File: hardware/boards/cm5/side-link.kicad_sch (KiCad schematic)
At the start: 2 parts, among them J201 05A20L24P

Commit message: feat(cm5): take the side link on a vertical FH12 at the right edge
J201 becomes a Hirose FH12-24S-0.5SVA(54), contacts toward the right edge with its lands 0.3 mm from it, pin 1 at the front end; main pin n still meets J201 pin 25 - n.
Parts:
- J201: value 05A20L24P -> FH12-24S-0.5SVA(54); footprint Iasis:HanElectricity_05A20L24P -> Iasis:Hirose_FH12-24S-0.5SVA_1x24-1MP_P0.50mm_Vertical; LCSC C5362158 -> C3169218; MPN 05A20L24P -> FH12-24S-0.5SVA(54); Manufacturer HanElectricity -> Hirose
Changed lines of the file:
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@@
 			(effects (font (size 1.27 1.27)) (justify left))
 		)
-		(property "Value" "05A20L24P"
+		(property "Value" "FH12-24S-0.5SVA(54)"
 			(at 99.06 101.6 0)
 			(show_name no)
@@
 			(effects (font (size 1.27 1.27)) (justify left))
 		)
-		(property "Footprint" "Iasis:HanElectricity_05A20L24P"
+		(property "Footprint" "Iasis:Hirose_FH12-24S-0.5SVA_1x24-1MP_P0.50mm_Vertical"
 			(at 101.6 99.06 0)
 			(hide yes)
@@
 			)
 		)
-		(property "LCSC" "C5362158"
+		(property "LCSC" "C3169218"
 			(at 101.6 99.06 0)
 			(hide yes)
@@
 			)
 		)
-		(property "MPN" "05A20L24P"
+		(property "MPN" "FH12-24S-0.5SVA(54)"
 			(at 101.6 99.06 0)
 			(hide yes)
@@
 			)
 		)
-		(property "Manufacturer" "HanElectricity"
+		(property "Manufacturer" "Hirose"
 			(at 101.6 99.06 0)
 			(hide yes)

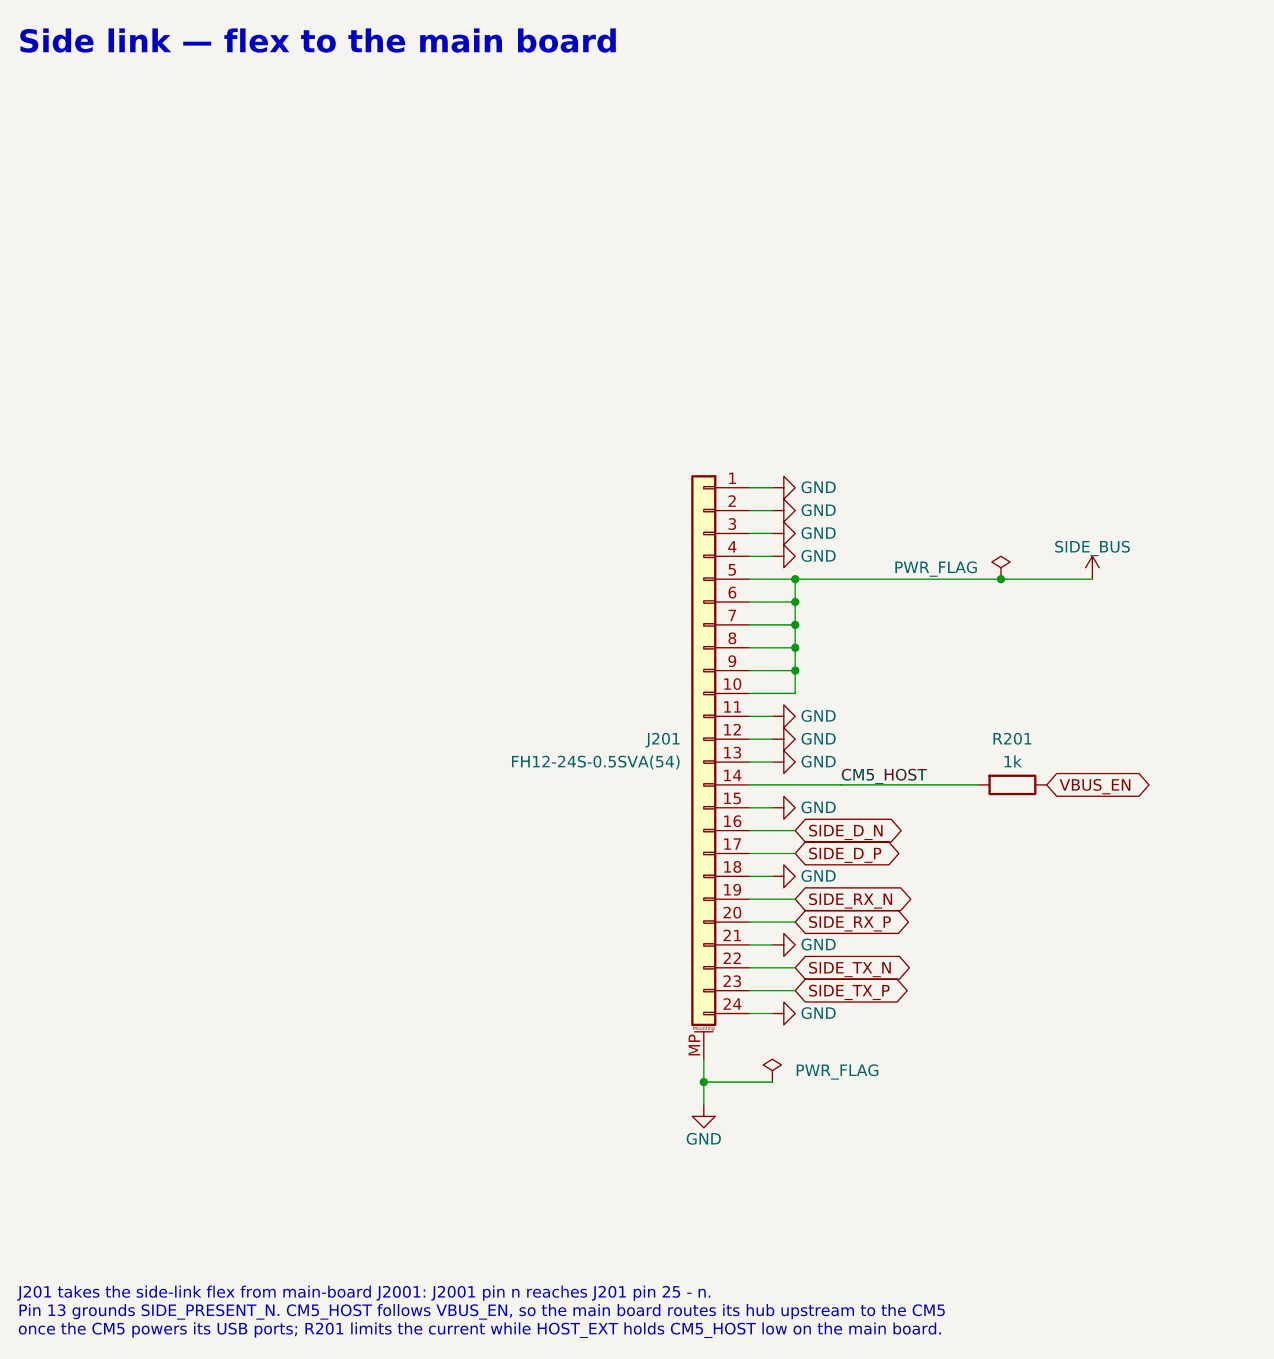
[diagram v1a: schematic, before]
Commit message: feat(hardware): use stocked CM5 headers
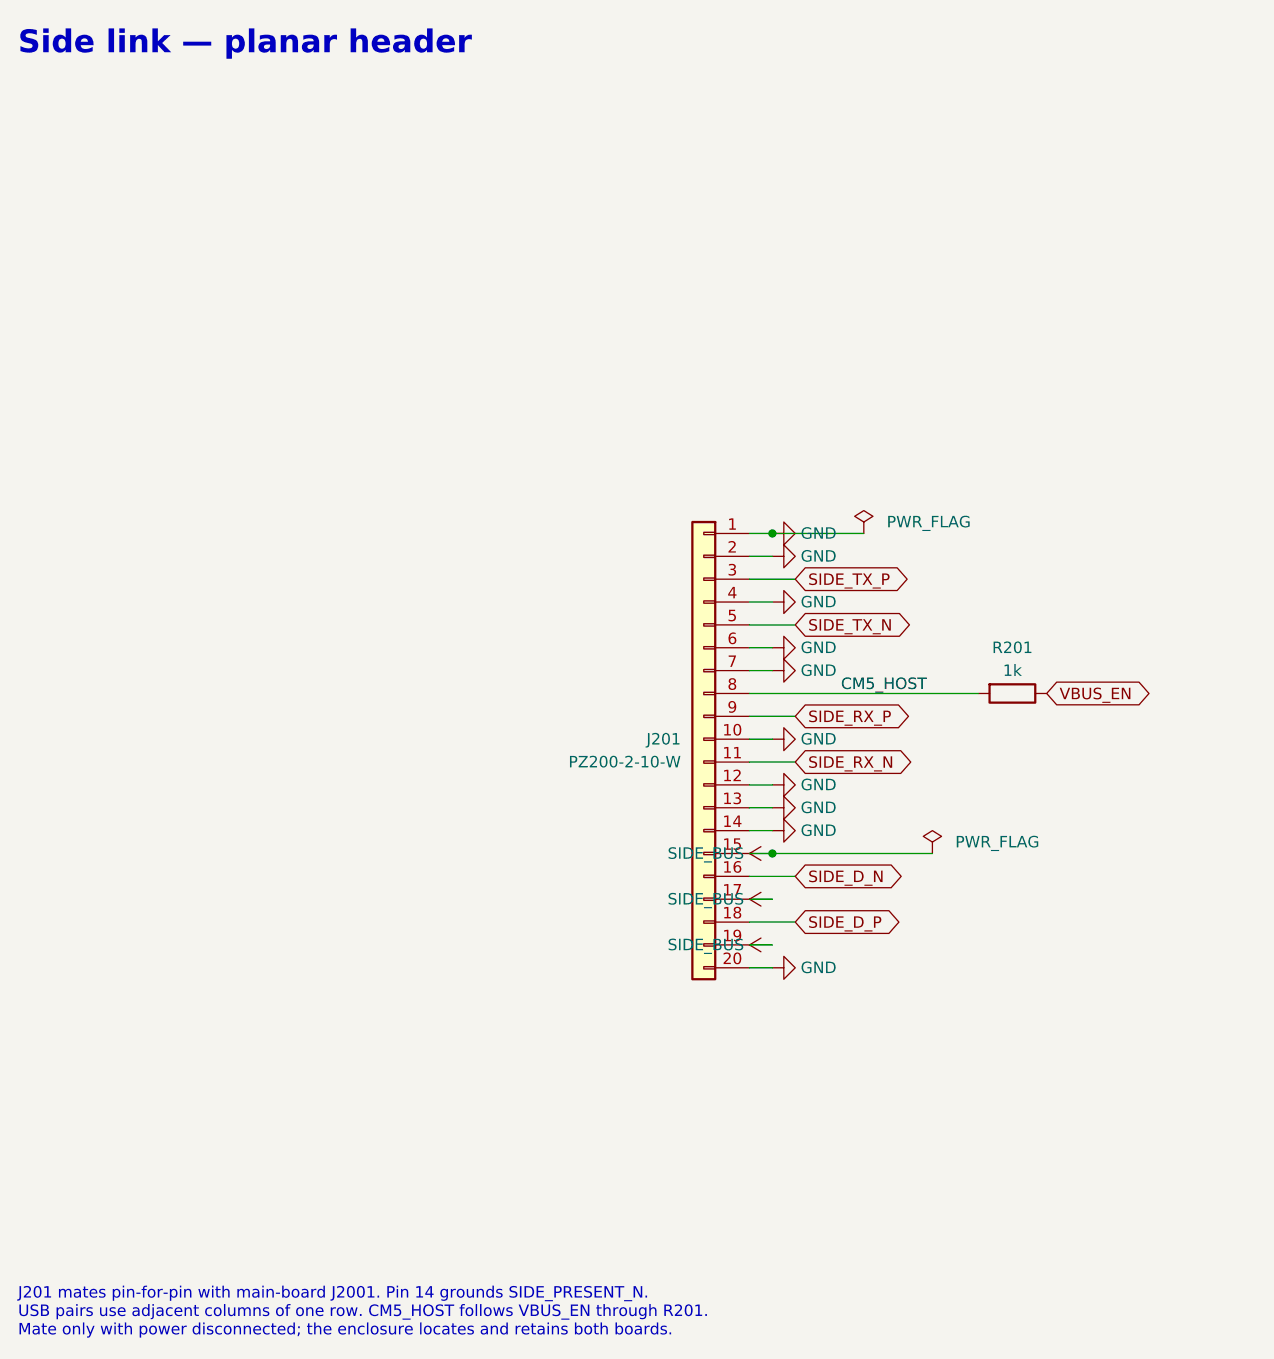
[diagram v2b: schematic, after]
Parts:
- J201: value FH12-24S-0.5SVA(54) -> PZ200-2-10-W; footprint Iasis:Hirose_FH12-24S-0.5SVA_1x24-1MP_P0.50mm_Vertical -> Connector_PinHeader_2.00mm:PinHeader_2x10_P2.00mm_Horizontal; symbol Connector_Generic_MountingPin:Conn_01x24_MountingPin -> Connector_Generic:Conn_01x20; LCSC C3169218 -> C2906016; MPN FH12-24S-0.5SVA(54) -> PZ200-2-10-W; Manufacturer Hirose -> HCTL
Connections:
- net CM5_HOST: now also J201.8 (Pin_8); no longer J201.14 (Pin_14)
- net GND: now also J201.10 (Pin_10), J201.14 (Pin_14), J201.20 (Pin_20), J201.6 (Pin_6), J201.7 (Pin_7); no longer J201.11 (Pin_11), J201.15 (Pin_15), J201.18 (Pin_18), J201.21 (Pin_21), J201.24 (Pin_24), J201.3 (Pin_3), J201.MP (MountPin)
- net SIDE_BUS: now also J201.15 (Pin_15), J201.17 (Pin_17), J201.19 (Pin_19); no longer J201.10 (Pin_10), J201.5 (Pin_5), J201.6 (Pin_6), J201.7 (Pin_7), J201.8 (Pin_8), J201.9 (Pin_9)
- net SIDE_D_P: now also J201.18 (Pin_18); no longer J201.17 (Pin_17)
- net SIDE_RX_N: now also J201.11 (Pin_11); no longer J201.19 (Pin_19)
- net SIDE_RX_P: now also J201.9 (Pin_9); no longer J201.20 (Pin_20)
- net SIDE_TX_N: now also J201.5 (Pin_5); no longer J201.22 (Pin_22)
- net SIDE_TX_P: now also J201.3 (Pin_3); no longer J201.23 (Pin_23)
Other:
- note added: "J201 mates pin-for-pin with main-board J2001. Pin 14 grounds SIDE_PRESENT_N. USB pairs use adjacent columns of one row. CM5_HOST follows VBUS_EN through R201. Mate only with power disconnected; the enclosure locates and retains both boards."
- note added: "Side link — planar header"
- note removed: "J201 takes the side-link flex from main-board J2001: J2001 pin n reaches J201 pin 25 - n. Pin 13 grounds SIDE_PRESENT_N. CM5_HOST follows VBUS_EN, so the main board routes its hub upstream to the CM5 once the CM5 powers its USB ports; R201 limits the current while HOST_EXT holds CM5_HOST low on the main board."
- note removed: "Side link — flex to the main board"
- title: Side link — flex to the main board -> Side link — planar header
- moved on the sheet: R201
